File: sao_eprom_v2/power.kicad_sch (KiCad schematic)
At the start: 35 parts, among them Q1 RE1C002UNTCL, Q2 RE1C002ZPTL, Q3 RE1C002UNTCL, Q4 RE1C002ZPTL, Q5 RE1C002UNTCL, Q6 RE1C002ZPTL, U10 AP3012, U8 SY8079AAC, U9 AP3012

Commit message: the experiment
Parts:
- C10, C11, C8, C9: footprint Capacitor_SMD:C_0603_1608Metric -> Capacitor_SMD:C_0603_1608Metric_Pad1.08x0.95mm_HandSolder
- C12, C13, C7: footprint Capacitor_SMD:C_0805_2012Metric -> Capacitor_SMD:C_0805_2012Metric_Pad1.18x1.45mm_HandSolder
- C5, C6: footprint Capacitor_SMD:C_0402_1005Metric -> Capacitor_SMD:C_0402_1005Metric_Pad0.74x0.62mm_HandSolder
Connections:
- net +3.3V is gone; now on net +3V3: C10.2, C8.2, L2.1, L3.1, U10.5 (IN), U9.5 (IN)

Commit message: Nearly finished the design
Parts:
- renumbered R20 to R1, R21 to R2
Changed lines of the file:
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@@
   (symbol (lib_id "Device:R") (at 139.7 97.79 90) (unit 1)
     (in_bom yes) (on_board yes) (dnp no) (fields_autoplaced)
-    (property "Reference" "R20" (at 139.7 91.44 90)
+    (property "Reference" "R1" (at 139.7 91.44 90)
       (effects (font (size 1.27 1.27)))
     )
@@
       (project "sao_eprom_v2"
         (path "/07beccdd-32b3-4f03-aa51-fb5544b6f2d4/e608ecd4-0557-4bb4-9ac0-2ae7e9dd9344"
-          (reference "R20") (unit 1)
+          (reference "R1") (unit 1)
         )
       )
@@
   (symbol (lib_id "Device:R") (at 143.51 85.09 0) (mirror y) (unit 1)
     (in_bom yes) (on_board yes) (dnp no)
-    (property "Reference" "R21" (at 140.97 83.8199 0)
+    (property "Reference" "R2" (at 140.97 83.8199 0)
       (effects (font (size 1.27 1.27)) (justify left))
     )
@@
       (project "sao_eprom_v2"
         (path "/07beccdd-32b3-4f03-aa51-fb5544b6f2d4/e608ecd4-0557-4bb4-9ac0-2ae7e9dd9344"
-          (reference "R21") (unit 1)
-        )
-      )
+          (reference "R2") (unit 1)
+        )
+      )

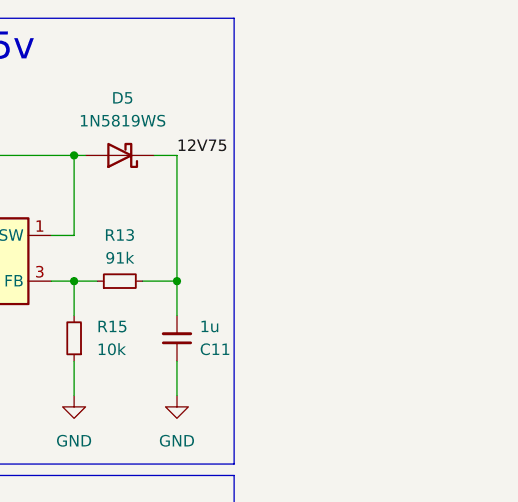
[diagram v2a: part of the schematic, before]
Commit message: Now with QWIIC and TestPads!
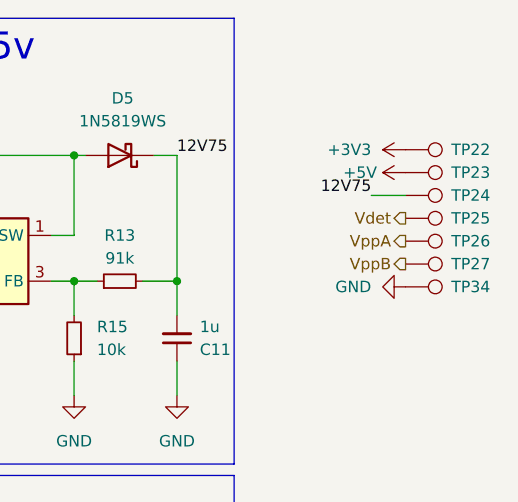
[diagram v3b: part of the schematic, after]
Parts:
- added TP22, TP23, TP24, TP25, TP26, TP27, TP34: TestPoint, TestPoint:TestPoint_Pad_D1.0mm, symbol Connector:TestPoint
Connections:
- net +3V3: now also TP22.1
- net +5V: now also TP23.1
- net 12V75: now also TP24.1
- net GND: now also TP34.1
- net Vdet: now also TP25.1
- net VppA: now also TP26.1
- net VppB: now also TP27.1

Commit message: Put yet another feedback in my design
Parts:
- D4, D5: footprint Diode_SMD:D_SOD-323 -> Diode_SMD:D_SOD-323_HandSoldering
- L1, L2, L3: footprint Inductor_SMD:L_0402_1005Metric_Pad0.77x0.64mm_HandSolder -> Inductor_SMD:L_0805_2012Metric_Pad1.15x1.40mm_HandSolder
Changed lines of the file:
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@@
       (effects (font (size 1.27 1.27)))
     )
-    (property "Footprint" "Inductor_SMD:L_0402_1005Metric_Pad0.77x0.64mm_HandSolder" (at 55.88 27.94 0)
+    (property "Footprint" "Inductor_SMD:L_0805_2012Metric_Pad1.15x1.40mm_HandSolder" (at 55.88 27.94 0)
       (effects (font (size 1.27 1.27)) hide)
     )
@@
       (effects (font (size 1.27 1.27)))
     )
-    (property "Footprint" "Diode_SMD:D_SOD-323" (at 162.56 23.495 0)
+    (property "Footprint" "Diode_SMD:D_SOD-323_HandSoldering" (at 162.56 23.495 0)
       (effects (font (size 1.27 1.27)) hide)
     )
@@
       (effects (font (size 1.27 1.27)))
     )
-    (property "Footprint" "Diode_SMD:D_SOD-323" (at 107.95 23.495 0)
+    (property "Footprint" "Diode_SMD:D_SOD-323_HandSoldering" (at 107.95 23.495 0)
       (effects (font (size 1.27 1.27)) hide)
     )
@@
       (effects (font (size 1.27 1.27)))
     )
-    (property "Footprint" "Inductor_SMD:L_0402_1005Metric_Pad0.77x0.64mm_HandSolder" (at 90.17 27.94 0)
+    (property "Footprint" "Inductor_SMD:L_0805_2012Metric_Pad1.15x1.40mm_HandSolder" (at 90.17 27.94 0)
       (effects (font (size 1.27 1.27)) hide)
     )
@@
       (effects (font (size 1.27 1.27)))
     )
-    (property "Footprint" "Inductor_SMD:L_0402_1005Metric_Pad0.77x0.64mm_HandSolder" (at 144.78 27.94 0)
-      (effects (font (size 1.27 1.27)) hide)
-    )
+    (property "Footprint" "Inductor_SMD:L_0805_2012Metric_Pad1.15x1.40mm_HandSolder" (at 144.78 27.94 0)
+      (effects (font (size 1.27 1.27)) hide)
+    )

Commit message: Candidate revision No. 1
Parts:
- renumbered TP34 to TP28
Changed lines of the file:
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@@
   (symbol (lib_id "Connector:TestPoint") (at 194.31 42.545 270) (unit 1)
     (in_bom yes) (on_board yes) (dnp no) (fields_autoplaced)
-    (property "Reference" "TP34" (at 199.39 42.545 90)
+    (property "Reference" "TP28" (at 199.39 42.545 90)
       (effects (font (size 1.27 1.27)) (justify left))
     )
@@
       (project "sao_eprom_v2"
         (path "/07beccdd-32b3-4f03-aa51-fb5544b6f2d4/e608ecd4-0557-4bb4-9ac0-2ae7e9dd9344"
-          (reference "TP34") (unit 1)
+          (reference "TP28") (unit 1)
         )
       )

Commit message: More EPROM devving
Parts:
- added Q7: RE1C002UNTCL, Package_TO_SOT_SMD:SOT-416, symbol Transistor_FET:2N7002E
- added Q8: RE1C002ZPTL, Package_TO_SOT_SMD:SOT-416, symbol Transistor_FET:AO3401A
- added R22: 100R, Resistor_SMD:R_0402_1005Metric_Pad0.72x0.64mm_HandSolder, symbol Device:R
- added R23: 1K, Resistor_SMD:R_0402_1005Metric_Pad0.72x0.64mm_HandSolder, symbol Device:R
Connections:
- net 12V75: now also Q8.2 (S), R23.1
- net GND: now also Q7.2 (S)
- new net: Q7.1 (G), R22.2
- new net: Q7.3 (D), Q8.1 (G), R23.2
- new net VLED: Q8.3 (D)
- new net VLEDEN: R22.1
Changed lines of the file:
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@@
   (junction (at 50.8 35.56) (diameter 0) (color 0 0 0 0)
   )
+  (junction (at 198.12 81.28) (diameter 0) (color 0 0 0 0)
+  )
   (junction (at 114.3 41.91) (diameter 0) (color 0 0 0 0)
   )
   (junction (at 125.73 27.94) (diameter 0) (color 0 0 0 0)
   )
+  (junction (at 205.74 91.44) (diameter 0) (color 0 0 0 0)
+  )
   (junction (at 88.9 80.01) (diameter 0) (color 0 0 0 0)
   )
@@
     (stroke (width 0) (type default))
   )
+  (wire (pts (xy 205.74 91.44) (xy 205.74 93.98))
+    (stroke (width 0) (type default))
+  )
   (wire (pts (xy 144.78 46.99) (xy 144.78 54.61))
     (stroke (width 0) (type default))
@@
     (stroke (width 0) (type default))
   )
+  (wire (pts (xy 205.74 91.44) (xy 205.74 88.9))
+    (stroke (width 0) (type default))
+  )
   (wire (pts (xy 71.12 27.94) (xy 77.47 27.94))
     (stroke (width 0) (type default))
@@
     (stroke (width 0) (type default))
   )
+  (wire (pts (xy 198.12 81.28) (xy 200.66 81.28))
+    (stroke (width 0) (type default))
+  )
   (wire (pts (xy 114.3 50.8) (xy 114.3 54.61))
     (stroke (width 0) (type default))
@@
     (stroke (width 0) (type default))
   )
+  (wire (pts (xy 198.12 91.44) (xy 205.74 91.44))
+    (stroke (width 0) (type default))
+  )
   (wire (pts (xy 34.29 90.17) (xy 41.91 90.17))
     (stroke (width 0) (type default))
@@
     (stroke (width 0) (type default))
   )
+  (wire (pts (xy 182.88 81.28) (xy 198.12 81.28))
+    (stroke (width 0) (type default))
+  )
   (wire (pts (xy 157.48 27.94) (xy 147.32 27.94))
     (stroke (width 0) (type default))
@@
     (stroke (width 0) (type default))
   )
+  (wire (pts (xy 198.12 82.55) (xy 198.12 81.28))
+    (stroke (width 0) (type default))
+  )
   (wire (pts (xy 143.51 90.17) (xy 151.13 90.17))
     (stroke (width 0) (type default))
@@
     (stroke (width 0) (type default))
   )
+  (wire (pts (xy 205.74 106.68) (xy 205.74 104.14))
+    (stroke (width 0) (type default))
+  )
+  (wire (pts (xy 198.12 91.44) (xy 198.12 90.17))
+    (stroke (width 0) (type default))
+  )
   (wire (pts (xy 100.33 41.91) (xy 102.87 41.91))
     (stroke (width 0) (type default))
@@
     (fill (type none))
   )
-  (rectangle (start 12.7 63.5) (end 175.26 113.03)
+  (rectangle (start 176.53 12.7) (end 229.87 62.23)
+    (stroke (width 0) (type default))
+    (fill (type none))
+  )
+  (rectangle (start 12.7 63.5) (end 229.87 113.03)
     (stroke (width 0) (type default))
     (fill (type none))
@@
     (effects (font (size 1.27 1.27)) (justify right bottom))
   )
+  (label "12V75" (at 182.88 81.28 0) (fields_autoplaced)
+    (effects (font (size 1.27 1.27)) (justify left bottom))
+  )
   (label "12V75" (at 128.27 80.01 0) (fields_autoplaced)
     (effects (font (size 1.27 1.27)) (justify left bottom))
@@
   (hierarchical_label "VppA" (shape output) (at 46.99 80.01 0) (fields_autoplaced)
     (effects (font (size 1.27 1.27)) (justify left))
+  )
+  (hierarchical_label "VLED" (shape output) (at 210.82 81.28 0) (fields_autoplaced)
+    (effects (font (size 1.27 1.27)) (justify left))
+  )
+  (hierarchical_label "VLEDEN" (shape input) (at 190.5 99.06 180) (fields_autoplaced)
+    (effects (font (size 1.27 1.27)) (justify right))
   )
   (hierarchical_label "VppBEN" (shape input) (at 81.28 97.79 180) (fields_autoplaced)
@@
     )
   )
+  (symbol (lib_name "GND_1") (lib_id "power:GND") (at 205.74 106.68 0) (unit 1)
+    (in_bom yes) (on_board yes) (dnp no) (fields_autoplaced)
+    (property "Reference" "#PWR019" (at 205.74 113.03 0)
+      (effects (font (size 1.27 1.27)) hide)
+    )
+    (property "Value" "GND" (at 205.74 111.76 0)
+      (effects (font (size 1.27 1.27)))
+    )
+    (property "Footprint" "" (at 205.74 106.68 0)
+      (effects (font (size 1.27 1.27)) hide)
+    )
+    (property "Datasheet" "" (at 205.74 106.68 0)
+      (effects (font (size 1.27 1.27)) hide)
+    )
+    (pin "1")
+    (instances
+      (project "sao_eprom_v2"
+        (path "/07beccdd-32b3-4f03-aa51-fb5544b6f2d4/e608ecd4-0557-4bb4-9ac0-2ae7e9dd9344"
+          (reference "#PWR019") (unit 1)
+        )
+      )
+      (project "sao_eprom"
+        (path "/23bd85f3-7065-4154-b889-dcac0f9110ff"
+          (reference "#PWR049") (unit 1)
+        )
+      )
+    )
+  )
+  (symbol (lib_id "Transistor_FET:2N7002E") (at 203.2 99.06 0) (unit 1)
+    (in_bom yes) (on_board yes) (dnp no) (fields_autoplaced)
+    (property "Reference" "Q7" (at 209.55 97.7899 0)
+      (effects (font (size 1.27 1.27)) (justify left))
+    )
+    (property "Value" "RE1C002UNTCL" (at 209.55 100.3299 0)
+      (effects (font (size 1.27 1.27)) (justify left))
+    )
+    (property "Footprint" "Package_TO_SOT_SMD:SOT-416" (at 208.28 100.965 0)
+      (effects (font (size 1.27 1.27) italic) (justify left) hide)
+    )
+    (property "Datasheet" "http://www.diodes.com/assets/Datasheets/ds30376.pdf" (at 203.2 99.06 0)
+      (effects (font (size 1.27 1.27)) (justify left) hide)
+    )
+    (pin "1")
+    (pin "2")
+    (pin "3")
+    (instances
+      (project "sao_eprom_v2"
+        (path "/07beccdd-32b3-4f03-aa51-fb5544b6f2d4/e608ecd4-0557-4bb4-9ac0-2ae7e9dd9344"
+          (reference "Q7") (unit 1)
+        )
+      )
+      (project "sao_eprom"
+        (path "/23bd85f3-7065-4154-b889-dcac0f9110ff"
+          (reference "Q1") (unit 1)
+        )
+      )
+    )
+  )
   (symbol (lib_id "Regulator_Switching:AP3012") (at 144.78 39.37 0) (unit 1)
     (in_bom yes) (on_board yes) (dnp no) (fields_autoplaced)
@@
     )
   )
+  (symbol (lib_id "Transistor_FET:AO3401A") (at 205.74 83.82 270) (mirror x) (unit 1)
+    (in_bom yes) (on_board yes) (dnp no) (fields_autoplaced)
+    (property "Reference" "Q8" (at 205.74 73.66 90)
+      (effects (font (size 1.27 1.27)))
+    )
+    (property "Value" "RE1C002ZPTL" (at 205.74 76.2 90)
+      (effects (font (size 1.27 1.27)))
+    )
+    (property "Footprint" "Package_TO_SOT_SMD:SOT-416" (at 203.835 78.74 0)
+      (effects (font (size 1.27 1.27) italic) (justify left) hide)
+    )
+    (property "Datasheet" "RE1C002ZPTL" (at 205.74 83.82 0)
+      (effects (font (size 1.27 1.27)) (justify left) hide)
+    )
+    (pin "1")
+    (pin "2")
+    (pin "3")
+    (instances
+      (project "sao_eprom_v2"
+        (path "/07beccdd-32b3-4f03-aa51-fb5544b6f2d4/e608ecd4-0557-4bb4-9ac0-2ae7e9dd9344"
+          (reference "Q8") (unit 1)
+        )
+      )
+      (project "sao_eprom"
+        (path "/23bd85f3-7065-4154-b889-dcac0f9110ff"
+          (reference "Q2") (unit 1)
+        )
+      )
+    )
+  )
   (symbol (lib_id "power:GND") (at 114.3 54.61 0) (unit 1)
     (in_bom yes) (on_board yes) (dnp no) (fields_autoplaced)
@@
     )
   )
+  (symbol (lib_id "Device:R") (at 198.12 86.36 0) (mirror y) (unit 1)
+    (in_bom yes) (on_board yes) (dnp no)
+    (property "Reference" "R23" (at 195.58 85.0899 0)
+      (effects (font (size 1.27 1.27)) (justify left))
+    )
+    (property "Value" "1K" (at 195.58 87.6299 0)
+      (effects (font (size 1.27 1.27)) (justify left))
+    )
+    (property "Footprint" "Resistor_SMD:R_0402_1005Metric_Pad0.72x0.64mm_HandSolder" (at 199.898 86.36 90)
+      (effects (font (size 1.27 1.27)) hide)
+    )
+    (property "Datasheet" "~" (at 198.12 86.36 0)
+      (effects (font (size 1.27 1.27)) hide)
+    )
+    (pin "1")
+    (pin "2")
+    (instances
+      (project "sao_eprom_v2"
+        (path "/07beccdd-32b3-4f03-aa51-fb5544b6f2d4/e608ecd4-0557-4bb4-9ac0-2ae7e9dd9344"
+          (reference "R23") (unit 1)
+        )
+      )
+      (project "sao_eprom"
+        (path "/23bd85f3-7065-4154-b889-dcac0f9110ff"
+          (reference "R11") (unit 1)
+        )
+      )
+    )
+  )
   (symbol (lib_id "power:GND") (at 194.31 42.545 270) (unit 1)
     (in_bom yes) (on_board yes) (dnp no) (fields_autoplaced)
@@
         )
       )
+    )
+  )
+  (symbol (lib_id "Device:R") (at 194.31 99.06 90) (unit 1)
+    (in_bom yes) (on_board yes) (dnp no) (fields_autoplaced)
+    (property "Reference" "R22" (at 194.31 92.71 90)
+      (effects (font (size 1.27 1.27)))
+    )
+    (property "Value" "100R" (at 194.31 95.25 90)
+      (effects (font (size 1.27 1.27)))
+    )
+    (property "Footprint" "Resistor_SMD:R_0402_1005Metric_Pad0.72x0.64mm_HandSolder" (at 194.31 100.838 90)
+      (effects (font (size 1.27 1.27)) hide)
+    )
+    (property "Datasheet" "~" (at 194.31 99.06 0)
+      (effects (font (size 1.27 1.27)) hide)
+    )
+    (pin "1")
+    (pin "2")
+    (instances
+      (project "sao_eprom_v2"
+        (path "/07beccdd-32b3-4f03-aa51-fb5544b6f2d4/e608ecd4-0557-4bb4-9ac0-2ae7e9dd9344"
+          (reference "R22") (unit 1)
+        )
+      )
+      (project "sao_eprom"
+        (path "/23bd85f3-7065-4154-b889-dcac0f9110ff"
+          (reference "R10") (unit 1)
+        )
+      )
